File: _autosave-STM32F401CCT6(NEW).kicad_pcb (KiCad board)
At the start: 2 copper layers, 37 parts, among them J1 USB_OTG, J2 Conn_02x03_Odd_Even, J3 Conn_01x20_des, J4 Conn_01x05_desc, J5 Conn_01x20, SW1 SW_Push, U1 MIC5219-3.3, U2 STM32F401CCT6, U3 USBLC6-2SC6, Y1 32.786K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

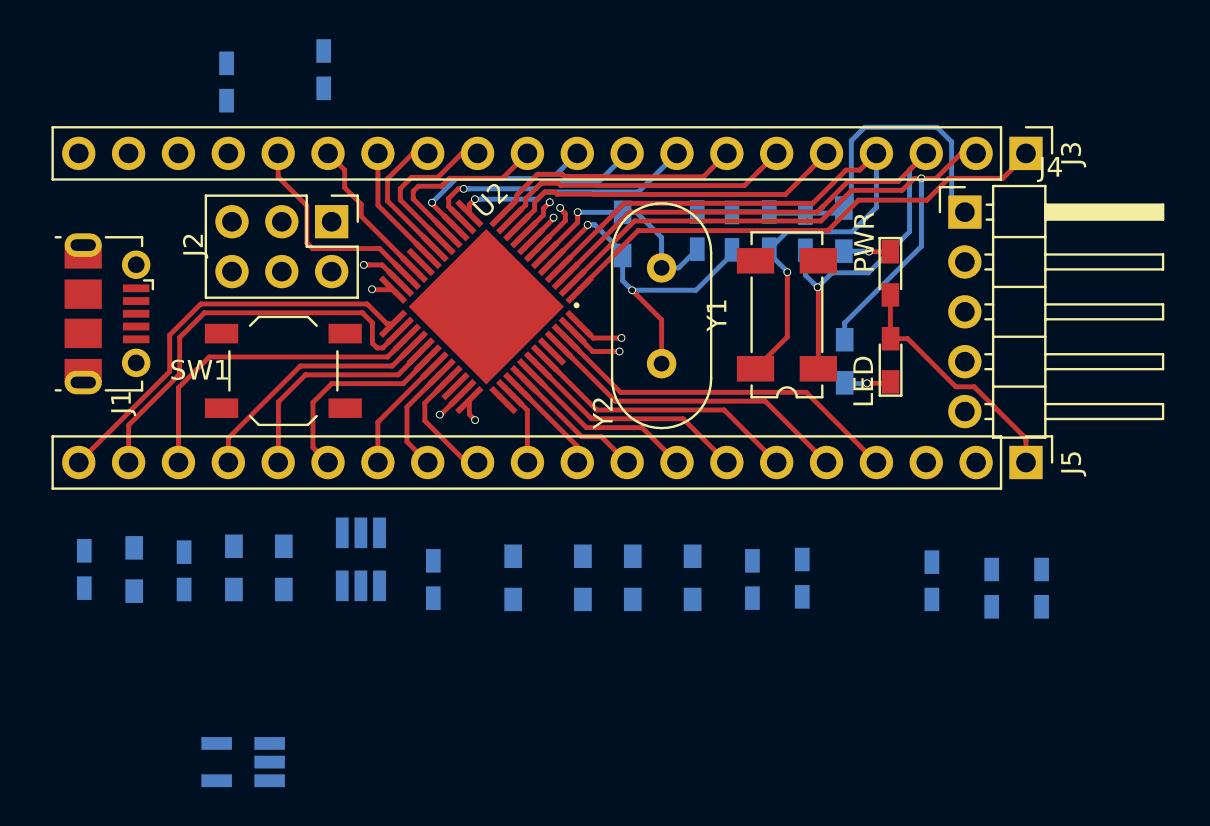
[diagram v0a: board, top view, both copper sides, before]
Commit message: Rerouted
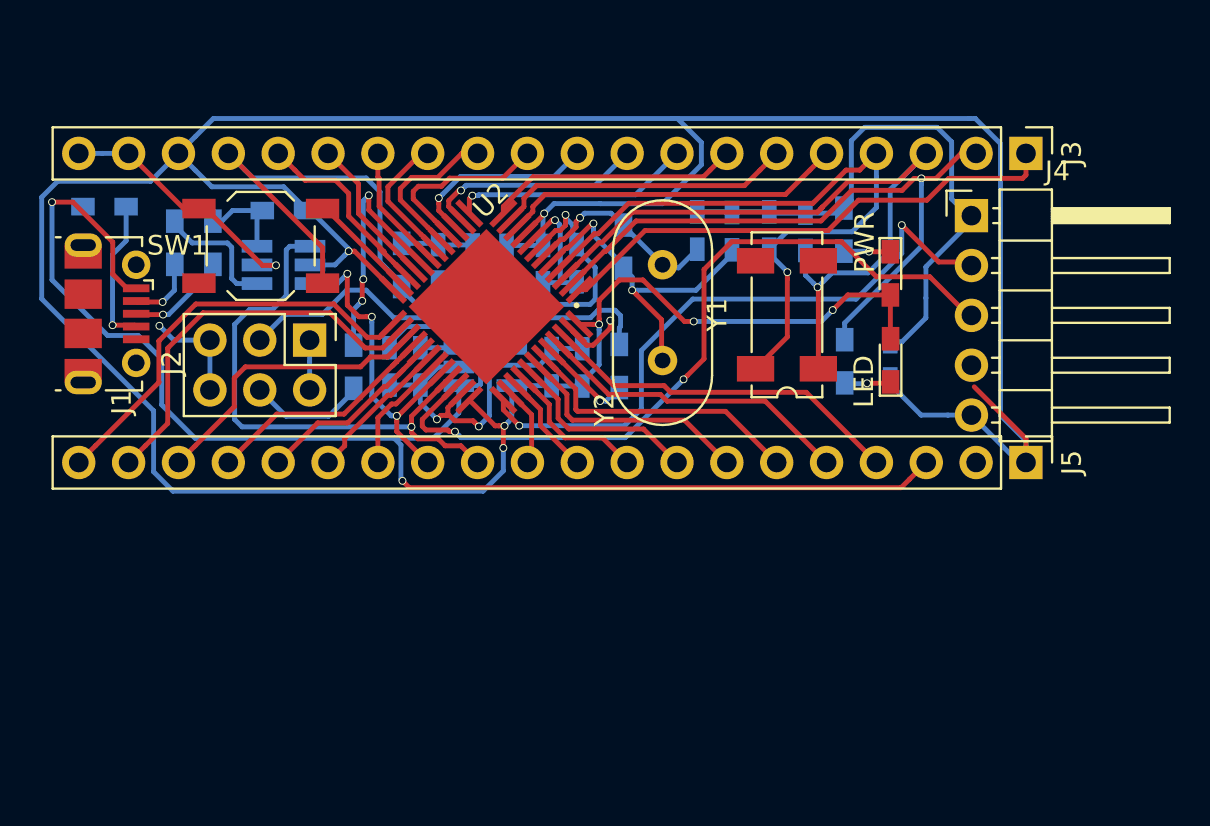
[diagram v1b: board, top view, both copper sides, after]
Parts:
- moved C14 42.4 mm to (117.4, 114.2), turned to 90 degrees
- moved C2 32.7 mm to (91.9, 114.5)
- moved R10 28.0 mm to (86.5, 106.5), turned to 0 degrees
- moved R4 27.4 mm to (82.9, 108.2)
- moved C4 26.0 mm to (101.7, 114.5)
- moved C3 25.4 mm to (101.4, 109.2), turned to 270 degrees
- moved U1 23.6 mm to (96.8, 114.5), turned to 0 degrees
- moved C5 22.2 mm to (100.2, 114.5), turned to 90 degrees
- moved C11 20.7 mm to (99.7, 109.3), turned to 270 degrees
- moved R9 20.5 mm to (77.4, 106.3), turned to 0 degrees
- moved C10 20.4 mm to (97.8, 109.3)
- moved R1 17.6 mm to (92.5, 109.3)
- moved R3 16.8 mm to (81.0, 108.2), turned to 270 degrees
- moved C12 16.1 mm to (94.4, 109.2), turned to 270 degrees
- moved C1 15.9 mm to (93.5, 114.5), turned to 270 degrees
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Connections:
- C14 pad 1: +5V -> VCC
- J4 pad 5: +5V -> VCC
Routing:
- net VCC: track 19.3 -> 194.1 mm, vias 4 -> 7
- net +5V: track 0.00 -> 74.5 mm, vias 0 -> 2
- net GND: track 29.1 -> 88.6 mm, vias 4 -> 6
- net /SWDIO: track 0.00 -> 39.0 mm, vias 0 -> 2
- net /RESET: track 2.74 -> 40.4 mm
- net /SWDCLK: track 0.00 -> 31.9 mm, vias 0 -> 2
- net /PA12: track 6.18 -> 28.4 mm, vias 0 -> 1
- net Net-(J2-Pad3): track 0.00 -> 21.9 mm
- net /BOOT1: track 0.00 -> 12.5 mm, vias 0 -> 3
- net /PA11: track 5.76 -> 17.2 mm, vias 0 -> 3
- net /ID: track 0.00 -> 7.56 mm, vias 0 -> 1
- net Net-(C2-Pad1): track 0.00 -> 7.27 mm
- net Net-(R3-Pad1): track 0.00 -> 6.53 mm
- net Net-(J2-Pad4): track 0.00 -> 6.01 mm
- net /D+: track 0.00 -> 5.16 mm, vias 0 -> 1
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
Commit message: rerouting (left reset)
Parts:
- moved R2 0.40 mm to (103.9, 108.8)
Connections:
- Y1 pad 2: /PC15 -> (no net)
- Y1 pad 4: (no net) -> /PC15
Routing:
- net GND: track 88.6 -> 212.5 mm, vias 6 -> 12
- net /RESET: track 40.4 -> 42.2 mm
- net VCC: track 194.1 -> 195.6 mm, vias 7 -> 9
- net Net-(R3-Pad1): track 6.53 -> 7.56 mm, vias 0 -> 2
- net Net-(J2-Pad3): track 21.9 -> 21.2 mm
- net /OSCIN: track 18.2 -> 17.5 mm
